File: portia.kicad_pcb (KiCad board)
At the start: 2 copper layers, 69.4 x 29.9 mm, 6 parts, among them U4 ESP32-WROOM

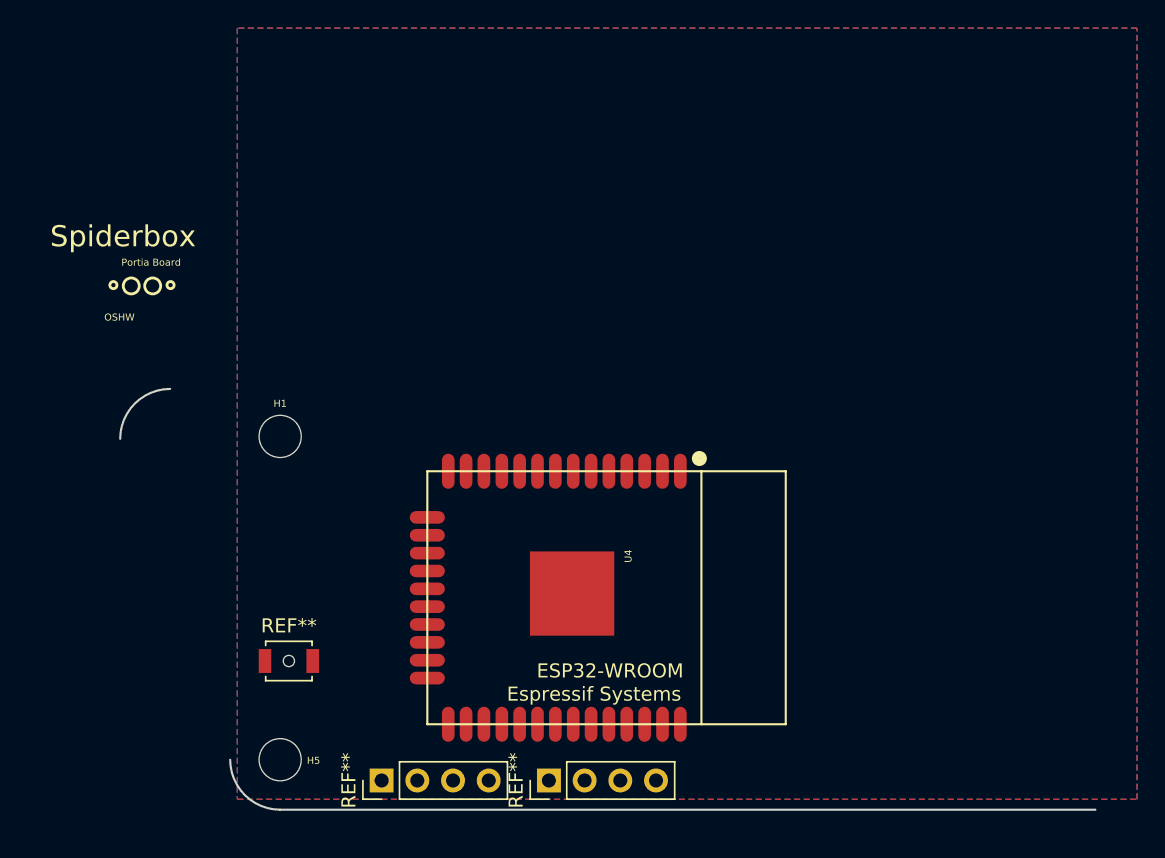
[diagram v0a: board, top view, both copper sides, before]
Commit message: update schematic
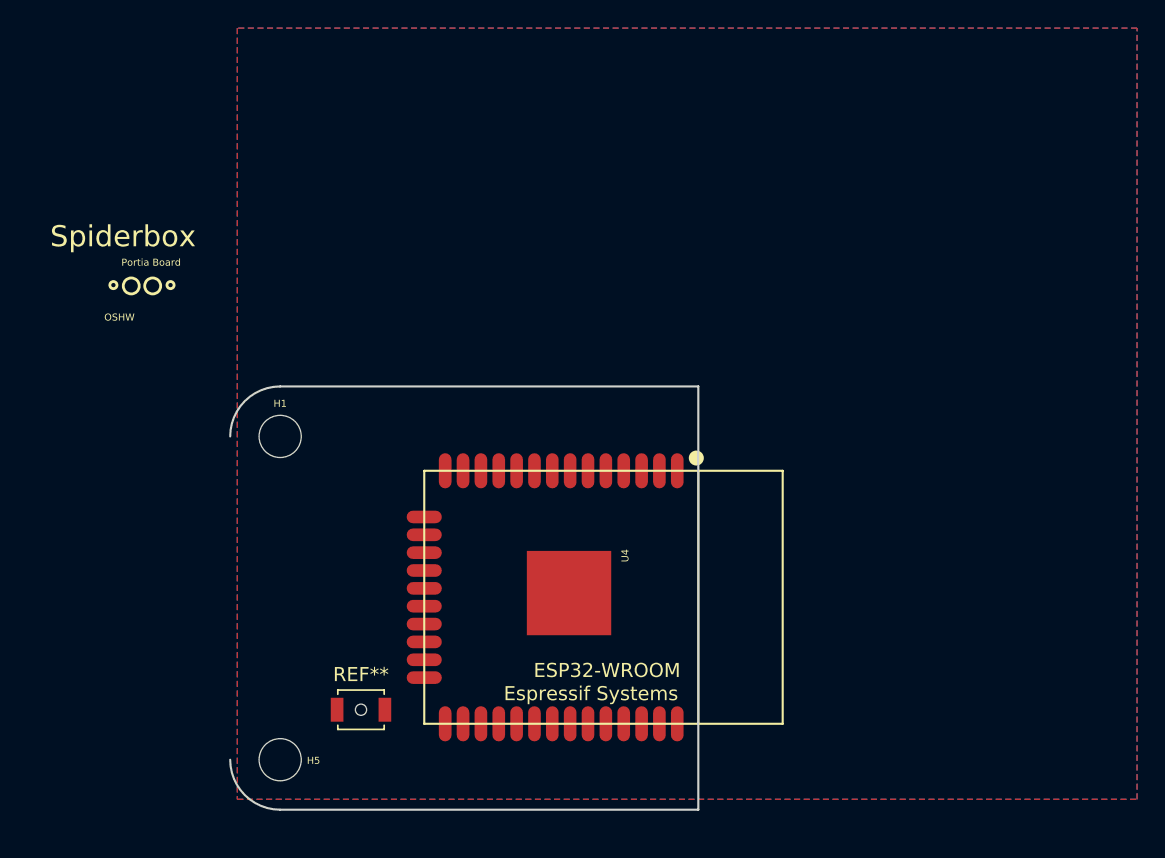
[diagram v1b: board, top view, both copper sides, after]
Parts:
- removed the REF** at (167.2, 131.8)
- removed the REF** at (179.1, 131.8)
- moved REF** 6.19 mm to (165.8, 126.7)
- moved U4 0.22 mm to (183.0, 118.7)
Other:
- board size 69.4 x 29.9 mm -> 33.3 x 30.1 mm
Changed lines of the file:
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@@
   (general
     (thickness 1.6)
-    (drawings 10)
+    (drawings 12)
     (tracks 0)
     (zones 0)
-    (modules 6)
+    (modules 4)
     (nets 37)
   )
@@
     (solder_mask_min_width 0.25)
     (aux_axis_origin 167.22 97.514)
-    (grid_origin 171.338 129.057)
+    (grid_origin 160.02 103.724)
     (visible_elements FFFFF77F)
     (pcbplotparams
@@
     (uvia_drill 0.1)
   )
-  (module Connector_PinHeader_2.54mm:PinHeader_1x04_P2.54mm_Vertical (layer F.Cu)
-    (at 167.238 131.757 90)
-    (descr "Through hole straight pin header, 1x04, 2.54mm pitch, single row")
-    (tags "Through hole pin header THT 1x04 2.54mm single row")
-    (fp_text reference REF** (at 0 -2.33 90) (layer F.SilkS)
-      (effects (font (size 1 1) (thickness 0.15)))
-    )
-    (fp_text value PinHeader_1x04_P2.54mm_Vertical (at 0 9.95 90) (layer F.Fab)
-      (effects (font (size 1 1) (thickness 0.15)))
-    )
-    (fp_line (start -0.635 -1.27) (end 1.27 -1.27) (layer F.Fab) (width 0.1))
-    (fp_line (start 1.27 -1.27) (end 1.27 8.89) (layer F.Fab) (width 0.1))
-    (fp_line (start 1.27 8.89) (end -1.27 8.89) (layer F.Fab) (width 0.1))
-    (fp_line (start -1.27 8.89) (end -1.27 -0.635) (layer F.Fab) (width 0.1))
-    (fp_line (start -1.27 -0.635) (end -0.635 -1.27) (layer F.Fab) (width 0.1))
-    (fp_line (start -1.33 8.95) (end 1.33 8.95) (layer F.SilkS) (width 0.12))
-    (fp_line (start -1.33 1.27) (end -1.33 8.95) (layer F.SilkS) (width 0.12))
-    (fp_line (start 1.33 1.27) (end 1.33 8.95) (layer F.SilkS) (width 0.12))
-    (fp_line (start -1.33 1.27) (end 1.33 1.27) (layer F.SilkS) (width 0.12))
-    (fp_line (start -1.33 0) (end -1.33 -1.33) (layer F.SilkS) (width 0.12))
-    (fp_line (start -1.33 -1.33) (end 0 -1.33) (layer F.SilkS) (width 0.12))
-    (fp_line (start -1.8 -1.8) (end -1.8 9.4) (layer F.CrtYd) (width 0.05))
-    (fp_line (start -1.8 9.4) (end 1.8 9.4) (layer F.CrtYd) (width 0.05))
-    (fp_line (start 1.8 9.4) (end 1.8 -1.8) (layer F.CrtYd) (width 0.05))
-    (fp_line (start 1.8 -1.8) (end -1.8 -1.8) (layer F.CrtYd) (width 0.05))
-    (fp_text user %R (at 0 3.81 180) (layer F.Fab)
-      (effects (font (size 1 1) (thickness 0.15)))
-    )
-    (pad 1 thru_hole rect (at 0 0 90) (size 1.7 1.7) (drill 1) (layers *.Cu *.Mask))
-    (pad 2 thru_hole oval (at 0 2.54 90) (size 1.7 1.7) (drill 1) (layers *.Cu *.Mask))
-    (pad 3 thru_hole oval (at 0 5.08 90) (size 1.7 1.7) (drill 1) (layers *.Cu *.Mask))
-    (pad 4 thru_hole oval (at 0 7.62 90) (size 1.7 1.7) (drill 1) (layers *.Cu *.Mask))
-    (model ${KISYS3DMOD}/Connector_PinHeader_2.54mm.3dshapes/PinHeader_1x04_P2.54mm_Vertical.wrl
-      (at (xyz 0 0 0))
-      (scale (xyz 1 1 1))
-      (rotate (xyz 0 0 0))
-    )
-  )
   (module ESP32-footprints-Lib:ESP32-WROOM (layer F.Cu)
-    (at 183.238 118.757 90)
+    (at 183.02 118.724 90)
     (fp_text reference U4 (at 2.96 1.546 90) (layer F.SilkS)
       (effects (font (size 0.5 0.5) (thickness 0.125)))
@@
     (pad 1 np_thru_hole circle (at 0 0) (size 3 3) (drill 3) (layers *.Cu *.Mask))
   )
-  (module Connector_PinHeader_2.54mm:PinHeader_1x04_P2.54mm_Vertical (layer F.Cu)
-    (at 179.138 131.757 90)
-    (descr "Through hole straight pin header, 1x04, 2.54mm pitch, single row")
-    (tags "Through hole pin header THT 1x04 2.54mm single row")
-    (fp_text reference REF** (at 0 -2.33 90) (layer F.SilkS)
-      (effects (font (size 1 1) (thickness 0.15)))
-    )
-    (fp_text value PinHeader_1x04_P2.54mm_Vertical (at 0 9.95 90) (layer F.Fab)
-      (effects (font (size 1 1) (thickness 0.15)))
-    )
-    (fp_text user %R (at 0 3.81 180) (layer F.Fab)
-      (effects (font (size 1 1) (thickness 0.15)))
-    )
-    (fp_line (start 1.8 -1.8) (end -1.8 -1.8) (layer F.CrtYd) (width 0.05))
-    (fp_line (start 1.8 9.4) (end 1.8 -1.8) (layer F.CrtYd) (width 0.05))
-    (fp_line (start -1.8 9.4) (end 1.8 9.4) (layer F.CrtYd) (width 0.05))
-    (fp_line (start -1.8 -1.8) (end -1.8 9.4) (layer F.CrtYd) (width 0.05))
-    (fp_line (start -1.33 -1.33) (end 0 -1.33) (layer F.SilkS) (width 0.12))
-    (fp_line (start -1.33 0) (end -1.33 -1.33) (layer F.SilkS) (width 0.12))
-    (fp_line (start -1.33 1.27) (end 1.33 1.27) (layer F.SilkS) (width 0.12))
-    (fp_line (start 1.33 1.27) (end 1.33 8.95) (layer F.SilkS) (width 0.12))
-    (fp_line (start -1.33 1.27) (end -1.33 8.95) (layer F.SilkS) (width 0.12))
-    (fp_line (start -1.33 8.95) (end 1.33 8.95) (layer F.SilkS) (width 0.12))
-    (fp_line (start -1.27 -0.635) (end -0.635 -1.27) (layer F.Fab) (width 0.1))
-    (fp_line (start -1.27 8.89) (end -1.27 -0.635) (layer F.Fab) (width 0.1))
-    (fp_line (start 1.27 8.89) (end -1.27 8.89) (layer F.Fab) (width 0.1))
-    (fp_line (start 1.27 -1.27) (end 1.27 8.89) (layer F.Fab) (width 0.1))
-    (fp_line (start -0.635 -1.27) (end 1.27 -1.27) (layer F.Fab) (width 0.1))
-    (pad 4 thru_hole oval (at 0 7.62 90) (size 1.7 1.7) (drill 1) (layers *.Cu *.Mask))
-    (pad 3 thru_hole oval (at 0 5.08 90) (size 1.7 1.7) (drill 1) (layers *.Cu *.Mask))
-    (pad 2 thru_hole oval (at 0 2.54 90) (size 1.7 1.7) (drill 1) (layers *.Cu *.Mask))
-    (pad 1 thru_hole rect (at 0 0 90) (size 1.7 1.7) (drill 1) (layers *.Cu *.Mask))
-    (model ${KISYS3DMOD}/Connector_PinHeader_2.54mm.3dshapes/PinHeader_1x04_P2.54mm_Vertical.wrl
-      (at (xyz 0 0 0))
-      (scale (xyz 1 1 1))
-      (rotate (xyz 0 0 0))
-    )
-  )
   (module Button_Switch_SMD:SW_SPST_B3U-1000P-B (layer F.Cu)
-    (at 160.638 123.257)
+    (at 165.77 126.724)
     (descr "Ultra-small-sized Tactile Switch with High Contact Reliability, Top-actuated Model, without Ground Terminal, with Boss")
     (tags "Tactile Switch")
@@
     )
   )
+  (gr_line (start 160.02 103.724) (end 189.77 103.724) (layer Edge.Cuts) (width 0.15))
+  (gr_line (start 189.77 133.836) (end 189.77 103.724) (layer Edge.Cuts) (width 0.15))
+  (gr_line (start 160.02 133.836) (end 189.77 133.836) (layer Edge.Cuts) (width 0.15))
   (gr_circle (center 148.156 96.514) (end 148.156 96.768) (layer F.SilkS) (width 0.2))
   (gr_circle (center 152.22 96.514) (end 152.22 96.768) (layer F.SilkS) (width 0.2))
@@
   )
   (gr_arc (start 160.02 130.28) (end 156.464 130.28) (angle -90) (layer Edge.Cuts) (width 0.15))
-  (gr_arc (start 152.194 107.457) (end 152.194 103.901) (angle -90) (layer Edge.Cuts) (width 0.15))
-  (gr_line (start 160.02 133.836) (end 218.02 133.836) (layer Edge.Cuts) (width 0.15))
+  (gr_arc (start 160.02 107.28) (end 160.02 103.724) (angle -90) (layer Edge.Cuts) (width 0.15))
   (zone (net 1) (net_name +3V3) (layer F.Cu) (hatch edge 0.508)
     (connect_pads (clearance 0.2))

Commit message: update layout
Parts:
- removed REF**: SW_SPST_B3U-1000P-B, Button_Switch_SMD:SW_SPST_B3U-1000P-B
- added D1: LED_ARGB, LED_SMD:LED_RGB_1210, F.Cu at (169.5, 125.8)
- added J1: Conn_01x02, Connector_PinHeader_2.54mm:PinHeader_1x02_P2.54mm_Vertical, F.Cu at (190.5, 105.8)
- added J2: Conn_01x02, Connector_PinHeader_2.54mm:PinHeader_1x02_P2.54mm_Vertical, F.Cu at (190.5, 131.8)
- added J3: Conn_02x08_Counter_Clockwise, Connector_PinHeader_2.54mm:PinHeader_2x08_P2.54mm_Vertical, F.Cu at (165.5, 106.3)
- added J4: Conn_02x06_Counter_Clockwise, Connector_PinHeader_2.54mm:PinHeader_2x06_P2.54mm_Vertical, F.Cu at (156.5, 112.4)
- added J5: Conn_02x08_Counter_Clockwise, Connector_PinHeader_2.54mm:PinHeader_2x08_P2.54mm_Vertical, F.Cu at (165.5, 133.7)
- added R1: R10, Resistor_SMD:R_0603_1608Metric, F.Cu at (165.5, 114.0)
- added R2: R60, Resistor_SMD:R_0603_1608Metric, F.Cu at (168.5, 114.0)
- added R3: R60, Resistor_SMD:R_0603_1608Metric, F.Cu at (165.5, 115.5)
- added R4: R10K, Resistor_SMD:R_0603_1608Metric, F.Cu at (169.0, 118.3)
- added R6: R10K, Resistor_SMD:R_0603_1608Metric, F.Cu at (169.0, 120.8)
- added SW1: Reset, Button_Switch_SMD:SW_SPST_B3U-1000P-B, F.Cu at (164.5, 123.8)
- added SW2: Reset, Button_Switch_SMD:SW_SPST_B3U-1000P-B, F.Cu at (164.5, 118.8)
- moved U4 2.75 mm to (185.8, 118.7)
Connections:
- U4 pad 3: /RESET -> Net-(R6-Pad1)
- U4 pad 33: /sda -> Net-(J5-Pad12)
- U4 pad 34: /rxd0 -> Net-(J5-Pad13)
- U4 pad 35: /txd0 -> Net-(J5-Pad14)
- U4 pad 36: /scl -> Net-(J5-Pad15)
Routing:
- removed copper zone on F.Cu, net +3V3
- removed copper zone on B.Cu, net GND
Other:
- board size 33.3 x 30.1 mm -> 36.1 x 30.1 mm

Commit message: layout redesign
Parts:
- J3, J5: value Conn_02x08_Counter_Clockwise -> Conn_02x08_Odd_Even
- J4: value Conn_02x06_Counter_Clockwise -> Conn_02x06_Odd_Even
- moved D1 22.4 mm to (147.8, 131.2)
- moved R1 18.5 mm to (147.0, 114.0)
- moved R2 18.5 mm to (150.0, 114.0)
- moved R3 18.5 mm to (147.0, 115.5)
- moved J3 18.0 mm to (183.3, 103.7), turned to 270 degrees
- moved SW1 13.2 mm to (166.2, 110.7)
- moved R6 10.1 mm to (170.1, 110.7), turned to 270 degrees
- moved R4 8.54 mm to (170.2, 126.7), turned to 90 degrees
- moved SW2 7.66 mm to (166.2, 126.2)
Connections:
- J3 pad 12: Net-(J3-Pad12) -> Net-(J3-Pad11)
- J3 pad 14: Net-(J3-Pad14) -> Net-(J3-Pad13)
- J3 pad 16: Net-(J3-Pad1) -> Net-(J3-Pad15)
- J3 pad 2: Net-(J3-Pad15) -> Net-(J3-Pad1)
- J3 pad 3: Net-(J3-Pad14) -> Net-(J3-Pad3)
- J3 pad 4: Net-(J3-Pad13) -> Net-(J3-Pad3)
- J3 pad 5: Net-(J3-Pad12) -> Net-(J3-Pad5)
- J3 pad 6: Net-(J3-Pad11) -> Net-(J3-Pad5)
- J3 pad 7: Net-(J3-Pad10) -> Net-(J3-Pad7)
- J3 pad 8: Net-(J3-Pad8) -> Net-(J3-Pad7)
- J3 pad 9: Net-(J3-Pad8) -> Net-(J3-Pad10)
- J4 pad 12: Net-(J4-Pad1) -> Net-(J4-Pad11)
- J4 pad 2: Net-(J4-Pad11) -> Net-(J4-Pad1)
- J4 pad 3: Net-(J4-Pad10) -> Net-(J4-Pad3)
- J4 pad 4: Net-(J4-Pad4) -> Net-(J4-Pad3)
- J4 pad 6: Net-(J4-Pad6) -> Net-(J4-Pad5)
- J4 pad 7: Net-(J4-Pad6) -> Net-(J4-Pad7)
- J4 pad 8: Net-(J4-Pad5) -> Net-(J4-Pad7)
- J4 pad 9: Net-(J4-Pad4) -> Net-(J4-Pad10)
- J5 pad 12: Net-(J5-Pad12) -> Net-(J5-Pad11)
- J5 pad 14: Net-(J5-Pad14) -> Net-(J5-Pad13)
- J5 pad 16: Net-(J5-Pad1) -> Net-(J5-Pad15)
- J5 pad 2: Net-(J5-Pad15) -> Net-(J5-Pad1)
- J5 pad 3: Net-(J5-Pad14) -> Net-(J5-Pad3)
- J5 pad 4: Net-(J5-Pad13) -> Net-(J5-Pad3)
- J5 pad 5: Net-(J5-Pad12) -> Net-(J5-Pad5)
- J5 pad 6: Net-(J5-Pad11) -> Net-(J5-Pad5)
- J5 pad 7: Net-(J5-Pad10) -> Net-(J5-Pad7)
- J5 pad 8: Net-(J5-Pad8) -> Net-(J5-Pad7)
- J5 pad 9: Net-(J5-Pad8) -> Net-(J5-Pad10)
- U4 pad 10: Net-(J3-Pad15) -> Net-(J3-Pad13)
- U4 pad 11: Net-(J3-Pad1) -> Net-(J3-Pad15)
- U4 pad 12: Net-(J4-Pad6) -> Net-(J4-Pad1)
- U4 pad 13: Net-(J4-Pad5) -> Net-(J4-Pad3)
- U4 pad 14: Net-(J4-Pad4) -> Net-(J4-Pad5)
- U4 pad 16: Net-(J4-Pad10) -> Net-(J4-Pad7)
- U4 pad 27: Net-(J4-Pad1) -> Net-(J4-Pad11)
- U4 pad 28: Net-(J4-Pad11) -> Net-(J4-Pad10)
- U4 pad 29: Net-(J5-Pad8) -> Net-(J5-Pad1)
- U4 pad 30: Net-(J5-Pad10) -> Net-(J5-Pad3)
- U4 pad 31: Net-(J5-Pad11) -> Net-(J5-Pad5)
- U4 pad 33: Net-(J5-Pad12) -> Net-(J5-Pad7)
- U4 pad 34: Net-(J5-Pad13) -> Net-(J5-Pad10)
- U4 pad 35: Net-(J5-Pad14) -> Net-(J5-Pad11)
- U4 pad 36: Net-(J5-Pad15) -> Net-(J5-Pad13)
- U4 pad 37: Net-(J5-Pad1) -> Net-(J5-Pad15)
- U4 pad 4: Net-(J3-Pad8) -> Net-(J3-Pad1)
- U4 pad 5: Net-(J3-Pad10) -> Net-(J3-Pad3)
- U4 pad 6: Net-(J3-Pad11) -> Net-(J3-Pad5)
- U4 pad 7: Net-(J3-Pad12) -> Net-(J3-Pad7)
- U4 pad 8: Net-(J3-Pad13) -> Net-(J3-Pad10)
- U4 pad 9: Net-(J3-Pad14) -> Net-(J3-Pad11)
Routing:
- net Net-(R6-Pad1): track 0.00 -> 25.1 mm
- net Net-(J5-Pad1): track 0.00 -> 23.4 mm, vias 0 -> 1
- net Net-(J5-Pad3): track 0.00 -> 20.0 mm, vias 0 -> 1
- net Net-(J3-Pad15): track 0.00 -> 19.9 mm, vias 0 -> 1
- net Net-(J5-Pad7): track 0.00 -> 18.8 mm, vias 0 -> 1
- net Net-(J5-Pad5): track 0.00 -> 18.8 mm, vias 0 -> 1
- net Net-(J3-Pad13): track 0.00 -> 18.6 mm, vias 0 -> 1
- net Net-(J5-Pad10): track 0.00 -> 18.5 mm, vias 0 -> 1
- net Net-(J3-Pad11): track 0.00 -> 17.6 mm, vias 0 -> 1
- net Net-(J5-Pad11): track 0.00 -> 17.1 mm, vias 0 -> 1
- net Net-(J5-Pad13): track 0.00 -> 16.9 mm, vias 0 -> 1
- net Net-(J5-Pad15): track 0.00 -> 16.3 mm, vias 0 -> 1
- net Net-(J3-Pad10): track 0.00 -> 16.1 mm, vias 0 -> 1
- net Net-(J3-Pad7): track 0.00 -> 15.3 mm, vias 0 -> 1
- net Net-(J3-Pad5): track 0.00 -> 14.4 mm, vias 0 -> 1
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
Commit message: update layout
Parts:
- removed D1: LED_ARGB, LED_SMD:LED_RGB_1210
- removed J1, J2: Conn_01x02, Connector_PinHeader_2.54mm:PinHeader_1x02_P2.54mm_Vertical
- removed J3, J5: Conn_02x08_Odd_Even, Connector_PinHeader_2.54mm:PinHeader_2x08_P2.54mm_Vertical
- removed J4: Conn_02x06_Odd_Even, Connector_PinHeader_2.54mm:PinHeader_2x06_P2.54mm_Vertical
- removed R1: R10, Resistor_SMD:R_0603_1608Metric
- removed R2, R3: R60, Resistor_SMD:R_0603_1608Metric
- moved SW2 10.4 mm to (175.1, 131.7)
- moved R4 10.0 mm to (178.8, 132.0)
- moved R6 7.24 mm to (175.3, 105.7)
- moved SW1 6.75 mm to (170.8, 105.7)
- moved U4 6.01 mm to (191.8, 118.7)
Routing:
- net Net-(R6-Pad1): track 25.1 -> 0.00 mm
- net Net-(J2-Pad11): track 23.4 -> 0.00 mm, vias 1 -> 0
- net Net-(J2-Pad10): track 20.0 -> 0.00 mm, vias 1 -> 0
- net Net-(J1-Pad1): track 19.9 -> 0.00 mm, vias 1 -> 0
- net Net-(J2-Pad8): track 18.8 -> 0.00 mm, vias 1 -> 0
- net Net-(J2-Pad9): track 18.8 -> 0.00 mm, vias 1 -> 0
- net Net-(J1-Pad2): track 18.6 -> 0.00 mm, vias 1 -> 0
- net Net-(J2-Pad7): track 18.5 -> 0.00 mm, vias 1 -> 0
- net Net-(J1-Pad3): track 17.6 -> 0.00 mm, vias 1 -> 0
- net Net-(J2-Pad6): track 17.1 -> 0.00 mm, vias 1 -> 0
- net Net-(J2-Pad5): track 16.9 -> 0.00 mm, vias 1 -> 0
- net Net-(J2-Pad4): track 16.3 -> 0.00 mm, vias 1 -> 0
- net Net-(J1-Pad4): track 16.1 -> 0.00 mm, vias 1 -> 0
- net Net-(J1-Pad5): track 15.3 -> 0.00 mm, vias 1 -> 0
- net Net-(J1-Pad6): track 14.4 -> 0.00 mm, vias 1 -> 0
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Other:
- board size 36.1 x 30.1 mm -> 42.3 x 30.6 mm
